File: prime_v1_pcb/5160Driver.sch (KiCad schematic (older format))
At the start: 36 parts, among them IC4 TMC5160A-TA-T, J14 Conn_01x04, J25 Conn_01x05, Q5 FDMC8030, Q6 FDMC8030, Q7 FDMC8030, Q8 FDMC8030

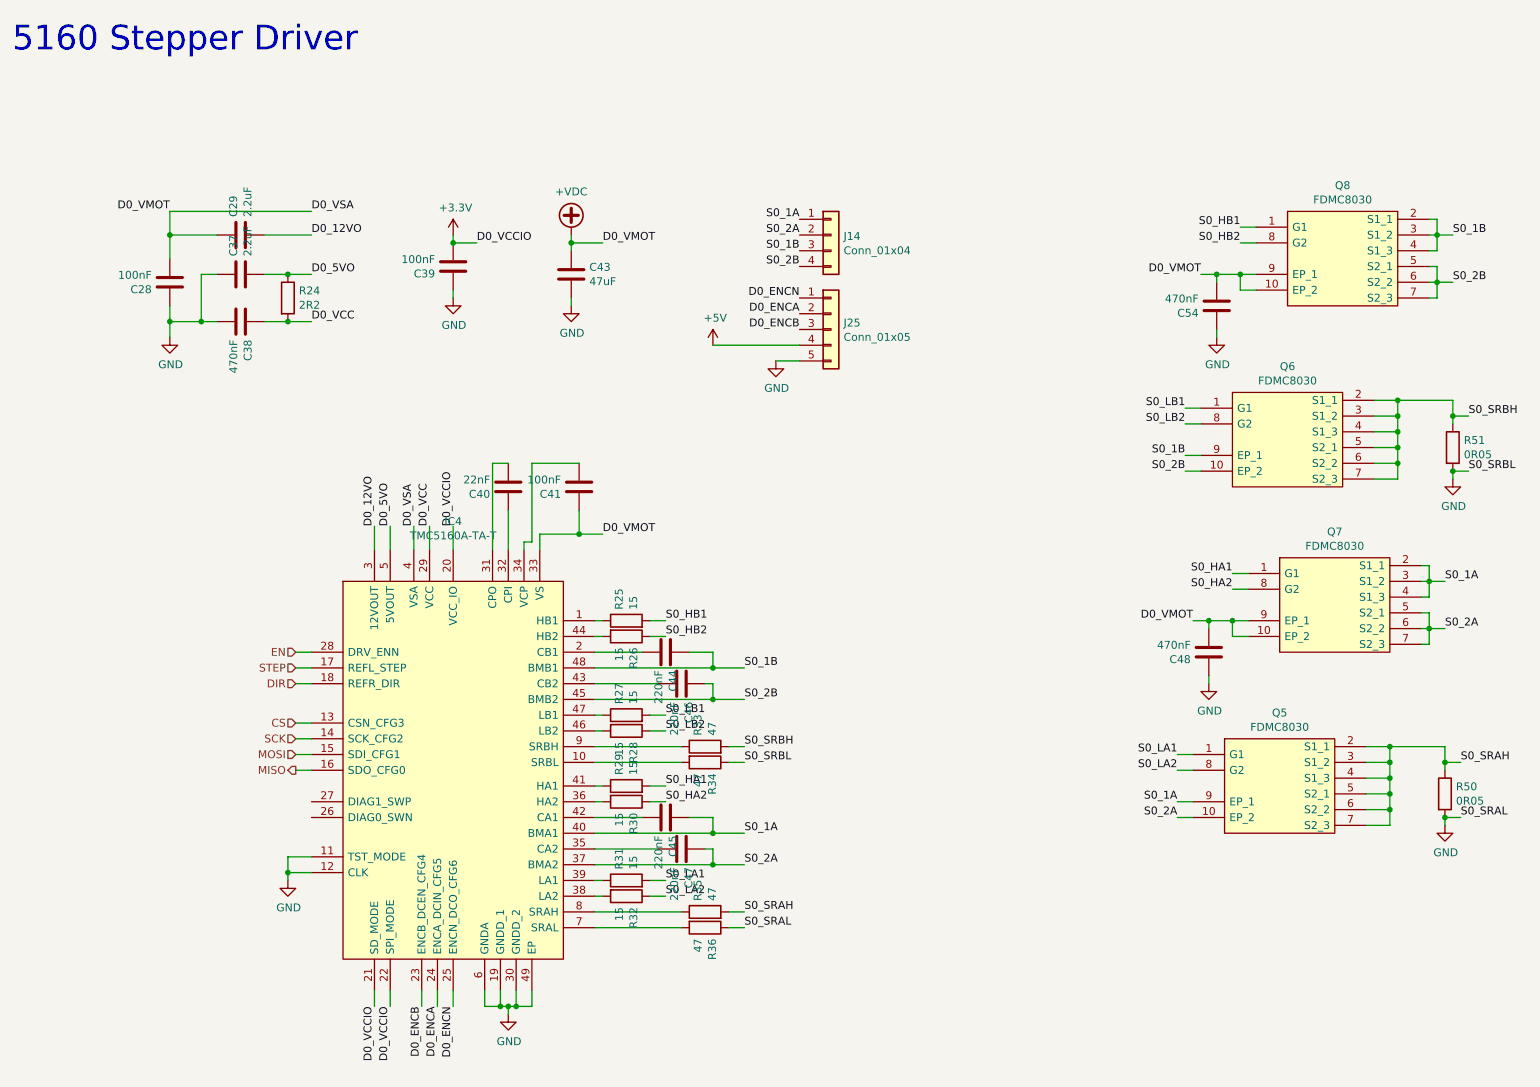
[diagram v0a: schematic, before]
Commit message: some work fixing board, bump arduino package version
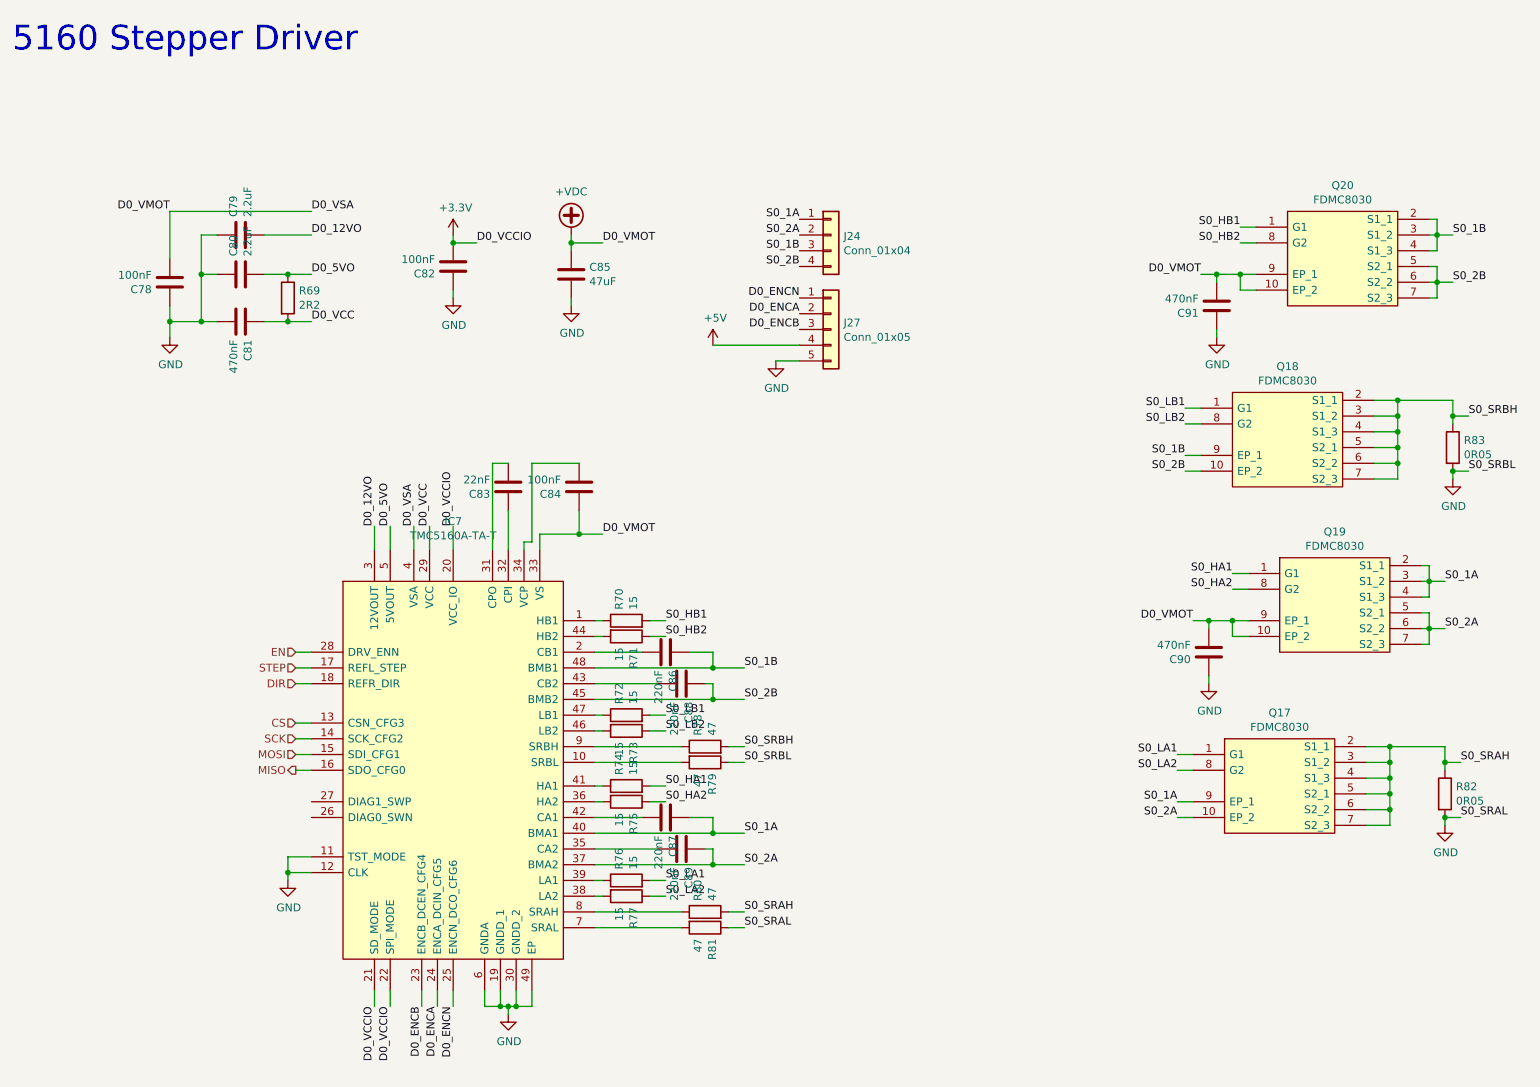
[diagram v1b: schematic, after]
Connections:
- net +VDC: no longer C29.1
- net GND: now also C29.1
